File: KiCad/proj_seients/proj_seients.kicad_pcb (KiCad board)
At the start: 4 copper layers, 102 parts, among them J1 BATERIA 12V, J10 Screw_Terminal_01x05, J11 FCarrera, J12 FCarrera, J13 FCarrera, J14 FCarrera, J17 FCarrera, J19 J_SENSOR_TEMP, J2 5f0857756ylz, J3 DE9_Pins, J4 Motor, J5 Motor, J6 Motor, J7 Manta_Asiento, J8 DE9_Socket, J9 FCarrera, Q1 IRLZ44N, SW1 SW_Push, SW2 SW_Push, SW3 SW_Push, SW4 SW_Push, SW5 SW_Push, SW6 SW_Push, SW7 SW_Push, U1 PIC24HJ128GP502, U10 MAX3232, U11 PCF8574AP, U2 LM2596S-5, U3 LM1117DT-3.3, U4 MCP2562-E-SN, U5 PCA9685BS, U6 DRV8871DDA, U7 DRV8871DDA, U8 DRV8871DDA, U9 24LC256, Y1 8MHz

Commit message: Versió 1.0 Layout
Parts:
- moved C36 137.7 mm to (182.5, 144.9), turned to -90 degrees
- moved C17 131.7 mm to (137.1, 147.0)
- moved C18 124.4 mm to (135.1, 143.0)
- moved C28 120.3 mm to (152.9, 140.5), turned to 180 degrees
- moved C19 119.3 mm to (96.5, 144.0)
- moved C20 118.2 mm to (89.0, 145.0)
- moved C24 117.9 mm to (147.1, 128.0)
- moved C21 113.5 mm to (106.5, 144.5)
- moved C22 111.2 mm to (125.5, 143.5)
- moved C6 100.1 mm to (134.6, 113.5)
- moved R2 98.5 mm to (184.0, 91.9), turned to 90 degrees
- moved C11 98.4 mm to (182.1, 81.5)
- moved R4 98.2 mm to (175.5, 145.1), turned to -90 degrees
- moved C7 97.7 mm to (158.9, 101.0), turned to 180 degrees
- moved R7 96.9 mm to (182.0, 140.0)
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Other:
- copper layers 4 -> 2

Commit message: Versió 1.1 Layout
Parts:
- moved C9 80.2 mm to (101.0, 122.5), turned to -90 degrees
- moved C10 72.0 mm to (110.0, 123.5), turned to -90 degrees
- moved C8 64.0 mm to (119.0, 123.5), turned to -90 degrees
- moved J7 49.1 mm to (82.3, 94.5), turned to -90 degrees
- moved C36 38.9 mm to (145.0, 134.6), turned to 90 degrees
- moved R6 32.3 mm to (148.5, 134.4), turned to 90 degrees
- moved R4 25.8 mm to (152.0, 134.4), turned to 90 degrees
- moved R25 19.7 mm to (155.5, 134.4), turned to 90 degrees
- moved U5 12.7 mm to (162.7, 130.5)
- moved SW5 10.0 mm to (123.5, 139.0)
- moved C1 9.73 mm to (126.5, 119.5)
- moved C22 9.00 mm to (116.5, 143.5)
- moved SW6 9.00 mm to (114.5, 139.3)
- moved Q1 2.77 mm to (125.5, 80.0)
- moved J1 1.00 mm to (81.0, 110.4)
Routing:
- net 5V: track 0.00 -> 142.6 mm, vias 0 -> 3
- net Net-(U11-P2): track 0.00 -> 87.9 mm, vias 0 -> 2
- net 12V: track 0.00 -> 85.6 mm
- net Net-(U11-P4): track 0.00 -> 78.0 mm
- net Net-(U11-P3): track 0.00 -> 71.2 mm, vias 0 -> 2
- net I2C_SDA: track 0.00 -> 70.1 mm, vias 0 -> 2
- net Net-(U11-P5): track 0.00 -> 63.9 mm
- net LIM_REC_MIN: track 0.00 -> 59.5 mm, vias 0 -> 2
- net I2C_SCL: track 0.00 -> 57.9 mm, vias 0 -> 2
- net LIM_REC_MAX: track 0.00 -> 53.0 mm
- net Net-(J7-Pin_1): track 0.00 -> 48.2 mm
- net LIM_POS_MAX: track 0.00 -> 43.3 mm, vias 0 -> 2
- net Net-(U1-AVSS): track 0.00 -> 38.2 mm
- net Net-(U11-P0): track 0.00 -> 32.5 mm
- net Net-(J10-Pin_1): track 0.00 -> 32.2 mm
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
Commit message: Versió 2.0 Layout
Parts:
- moved J6 113.7 mm to (81.6, 133.0), turned to -90 degrees
- moved SW1 111.4 mm to (188.2, 127.5), turned to 0 degrees
- moved R5 103.5 mm to (188.5, 140.1), turned to -90 degrees
- moved SW3 85.9 mm to (173.0, 104.5), turned to 0 degrees
- moved J5 85.3 mm to (111.7, 142.9), turned to 0 degrees
- moved U6 83.9 mm to (100.1, 134.0), turned to 180 degrees
- moved R7 76.5 mm to (106.0, 131.1), turned to 90 degrees
- moved J4 74.8 mm to (126.2, 142.9), turned to 0 degrees
- moved SW2 73.1 mm to (158.8, 132.2), turned to 180 degrees
- moved C21 71.6 mm to (175.7, 126.1), turned to 90 degrees
- moved C19 69.3 mm to (158.5, 113.0), turned to -90 degrees
- moved SW4 67.2 mm to (170.5, 128.5), turned to 180 degrees
- moved C22 66.8 mm to (177.7, 116.7), turned to 90 degrees
- moved C20 62.7 mm to (149.5, 128.3), turned to -90 degrees
- moved SW6 62.5 mm to (173.5, 118.8), turned to 180 degrees
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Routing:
- net 5V: track 142.6 -> 0.00 mm, vias 3 -> 0
- net Net-(U11-P2): track 87.9 -> 0.00 mm, vias 2 -> 0
- net 12V: track 85.6 -> 0.00 mm
- net Net-(U11-P4): track 78.0 -> 0.00 mm
- net Net-(U11-P3): track 71.2 -> 0.00 mm, vias 2 -> 0
- net I2C_SDA: track 70.1 -> 0.00 mm, vias 2 -> 0
- net Net-(U11-P5): track 63.9 -> 0.00 mm
- net LIM_REC_MIN: track 59.5 -> 0.00 mm, vias 2 -> 0
- net I2C_SCL: track 57.9 -> 0.00 mm, vias 2 -> 0
- net LIM_REC_MAX: track 53.0 -> 0.00 mm
- net Net-(J7-Pin_1): track 48.2 -> 0.00 mm
- net LIM_POS_MAX: track 43.3 -> 0.00 mm, vias 2 -> 0
- net Net-(U1-AVSS): track 38.2 -> 0.00 mm
- net Net-(U11-P0): track 32.5 -> 0.00 mm
- net Net-(J10-Pin_1): track 32.2 -> 0.00 mm
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- added copper zone on B.Cu, net GND
- added copper zone on F.Cu, net GND

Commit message: Versió 2.1 Layout
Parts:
- moved C22 11.0 mm to (188.8, 117.0)
- moved SW3 10.6 mm to (183.2, 107.2)
- moved SW6 9.17 mm to (182.5, 120.5)
- moved C6 5.78 mm to (131.4, 108.7), turned to 90 degrees
- moved U9 4.27 mm to (169.0, 108.0)
- moved C17 3.45 mm to (168.3, 139.2), turned to 0 degrees
- moved C5 1.50 mm to (131.5, 102.0)
- moved R1 1.22 mm to (142.8, 112.9), turned to 90 degrees
- moved C24 1.00 mm to (143.8, 127.0)
- moved C19 0.70 mm to (159.2, 113.0)
- moved R23 0.67 mm to (152.0, 112.7), turned to -90 degrees
- moved R16 0.52 mm to (147.4, 112.9), turned to 90 degrees
- moved D1 0.51 mm to (93.0, 123.5)
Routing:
- net 3.3V: track 0.00 -> 416.8 mm, vias 0 -> 2
- net 5V: track 0.00 -> 177.9 mm
- net 12V: track 0.00 -> 136.5 mm
- net Net-(J10-Pin_1): track 0.00 -> 109.0 mm, vias 0 -> 4
- net I2C_SDA: track 0.00 -> 94.7 mm, vias 0 -> 5
- net I2C_SCL: track 0.00 -> 86.4 mm, vias 0 -> 2
- net CALEFACCIÓ: track 0.00 -> 78.7 mm, vias 0 -> 3
- net LIM_POS_MIN: track 0.00 -> 73.5 mm, vias 0 -> 2
- net LIM_AL_MIN: track 0.00 -> 70.1 mm, vias 0 -> 1
- net Net-(U11-P1): track 0.00 -> 52.7 mm, vias 0 -> 1
- net LIM_REC_MAX: track 0.00 -> 52.4 mm, vias 0 -> 1
- net LIM_REC_MIN: track 0.00 -> 51.8 mm, vias 0 -> 2
- net Net-(J7-Pin_1): track 0.00 -> 48.2 mm
- net CINT: track 0.00 -> 47.6 mm, vias 0 -> 2
- net Net-(U1-AVSS): track 0.00 -> 46.5 mm
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
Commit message: Versió 2.2 Layout
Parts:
- J3: footprint Connector_Dsub:DSUB-9_Pins_Vertical_P2.77x2.84mm -> Connector_Dsub:DSUB-9_Pins_Horizontal_P2.77x2.84mm_EdgePinOffset9.40mm
- J8: footprint Connector_Dsub:DSUB-9_Socket_Vertical_P2.77x2.84mm -> Connector_Dsub:DSUB-9_Socket_Horizontal_P2.77x2.84mm_EdgePinOffset9.40mm
- moved J8 12.9 mm to (151.9, 78.3), turned to 180 degrees
- moved J3 5.01 mm to (187.0, 94.8)
- moved REF** 3.10 mm to (197.1, 149.1)
- moved REF** 3.01 mm to (78.8, 149.0)
- moved REF** 0.80 mm to (79.0, 67.7)
- moved REF** 0.30 mm to (197.0, 68.2)
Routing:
- net RX: track 45.2 -> 40.0 mm
- net CAN_H: track 30.0 -> 24.8 mm
- net CAN_L: track 27.1 -> 22.0 mm
- net TX: track 37.3 -> 39.3 mm
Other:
- board text added: "23/3/2026"
- board text added: "Autors: Miguel Tovar i Pol Salas PCB del circuit"
- board text added: "Placa de Control - Seients Elèctrics"
- board text added: "V2.2"

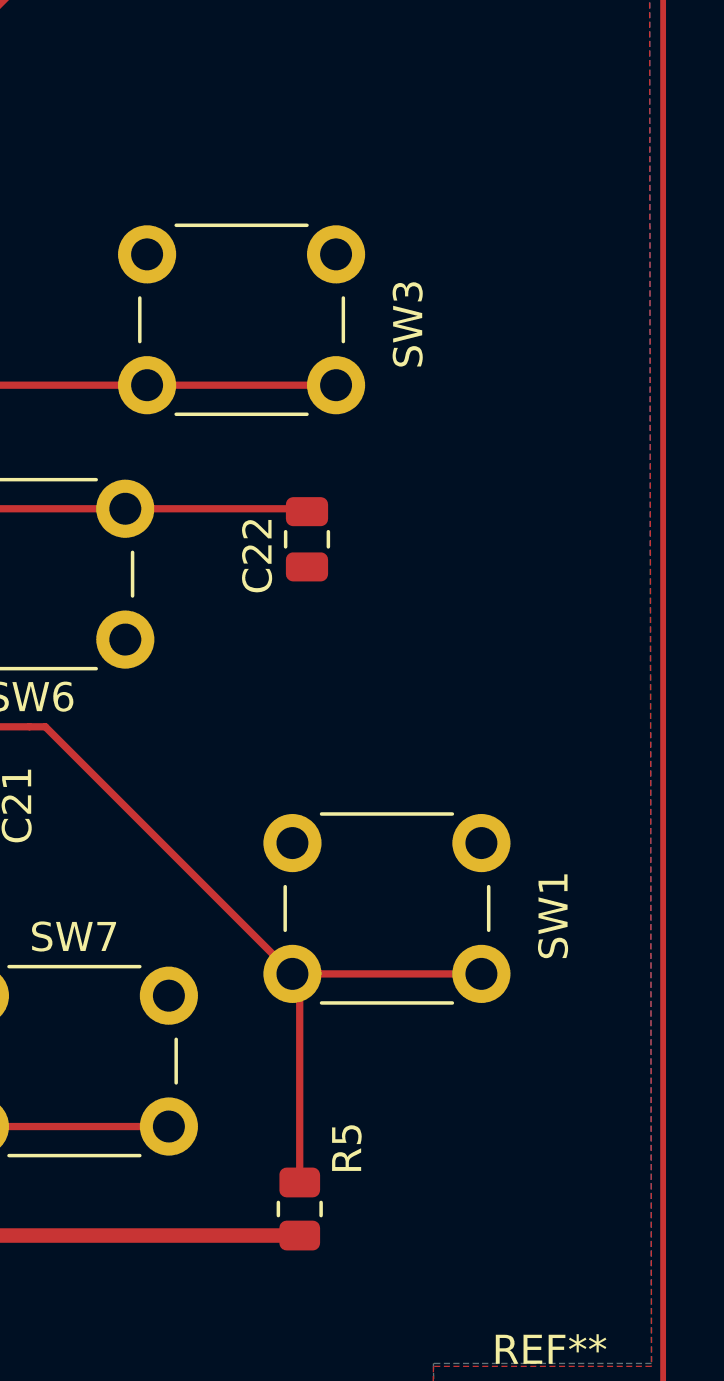
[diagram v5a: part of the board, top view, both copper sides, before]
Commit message: Afegit títol i autors a la placa
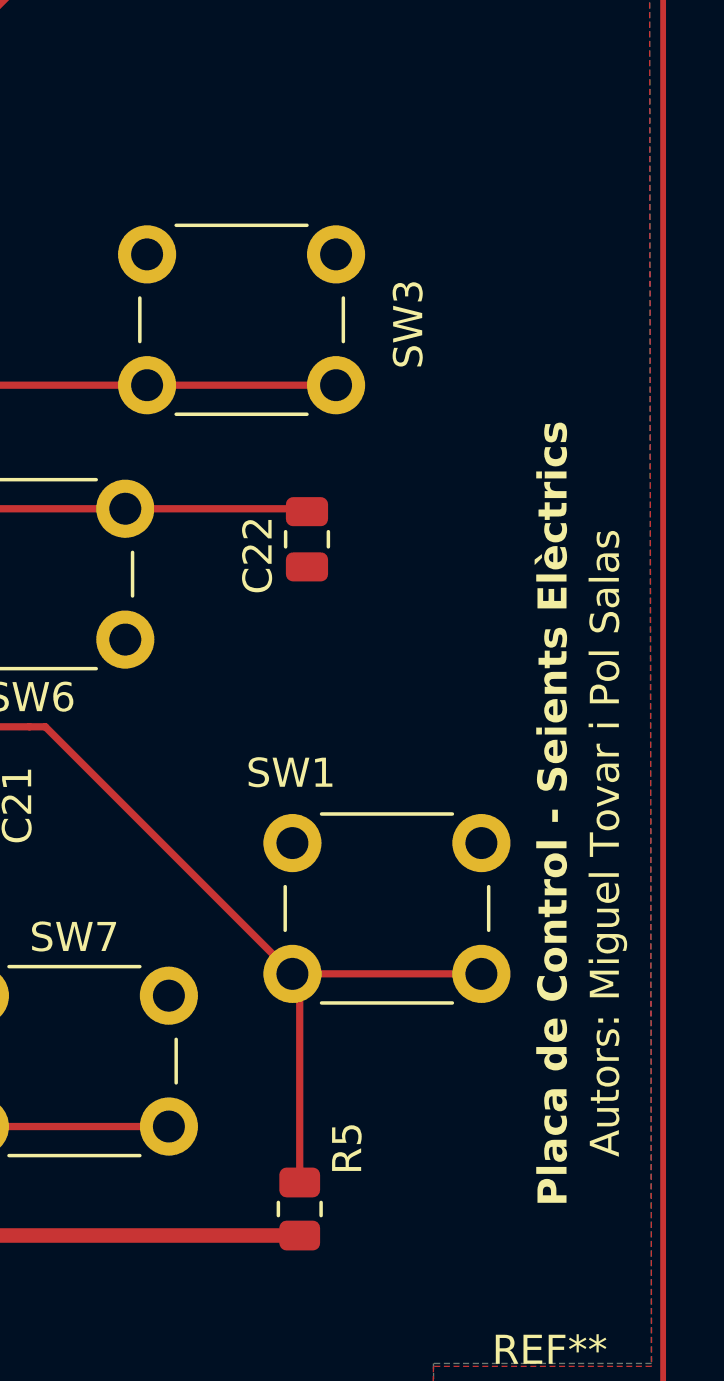
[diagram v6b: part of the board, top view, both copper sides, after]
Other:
- board text added: "Autors: Miguel Tovar i Pol Salas"
- board text removed: "23/3/2026"
- board text removed: "Autors: Miguel Tovar i Pol Salas PCB del circuit"
- board text removed: "V2.2"
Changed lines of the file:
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@@
 		(tags "tact sw push 6mm")
 		(property "Reference" "SW1"
-			(at 9 2.5 90)
+			(at -0.05 -2.4 180)
 			(layer "F.SilkS")
 			(effects
@@
 		(layer "F.Cu")
 	)
-	(gr_text "V2.2"
-		(at 268.5 194.2 0)
-		(layer "Cmts.User")
+	(gr_text "Placa de Control - Seients Elèctrics"
+		(at 197.8 140 90)
+		(layer "F.SilkS")
 		(effects
 			(font
-				(size 1.5 1.5)
-				(thickness 0.3)
+				(size 1 1)
+				(thickness 0.25)
 				(bold yes)
 			)
@@
 		)
 	)
-	(gr_text "23/3/2026\n"
-		(at 206.8 194.1 0)
-		(layer "Cmts.User")
+	(gr_text "Autors: Miguel Tovar i Pol Salas\n"
+		(at 199.6 138.3 90)
+		(layer "F.SilkS")
 		(effects
 			(font
-				(size 1.5 1.5)
-				(thickness 0.3)
-				(bold yes)
+				(size 1 1)
+				(thickness 0.25)
 			)
 			(justify left bottom)
-		)
-	)
-	(gr_text "Autors: Miguel Tovar i Pol Salas\nPCB del circuit"
-		(at 177.9 178.3 0)
-		(layer "Cmts.User")
-		(effects
-			(font
-				(size 3 3)
-				(thickness 0.75)
-			)
-			(justify left bottom)
-		)
-	)
-	(gr_text "Placa de Control - Seients Elèctrics"
-		(at 186.5 190.4 0)
-		(layer "Cmts.User")
-		(effects
-			(font
-				(size 1.5 1.5)
-				(thickness 0.3)
-				(bold yes)
-			)
-			(justify left bottom)

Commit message: Version V2.4
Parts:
- moved U10 1.17 mm to (164.0, 88.5)
- moved C7 1.05 mm to (160.0, 101.0)
- moved U4 1.00 mm to (166.5, 98.5)
- turned C20 to 90 degrees
- turned R9 to 90 degrees
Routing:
- net I2C_SCL: track 86.4 -> 101.0 mm, vias 2 -> 3
- net I2C_SDA: track 94.7 -> 104.0 mm, vias 5 -> 6
- net 5V: track 177.9 -> 170.0 mm
- net Net-(J7-Pin_1): track 48.2 -> 55.2 mm
- net Net-(U6-ILIM): track 0.00 -> 3.06 mm
- net 3.3V: track 416.8 -> 414.3 mm
- net Net-(D3-A): track 0.00 -> 2.50 mm
- net UART_RX: track 25.7 -> 27.0 mm
- net UART_TX: track 23.9 -> 25.2 mm
- net Net-(U10-VS+): track 4.41 -> 3.16 mm
- net Net-(U10-C2-): track 4.38 -> 3.12 mm
- net Net-(U10-C2+): track 4.64 -> 3.38 mm
- net Net-(U1-VCAP): track 3.88 -> 4.93 mm
- net CAN_H: track 24.8 -> 23.8 mm
- net CAN_L: track 22.0 -> 21.0 mm
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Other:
- board outline added: 126 x 89.4 mm

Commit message: V2.5
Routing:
- net 5V: track 170.0 -> 177.1 mm
- net Net-(J7-Pin_1): track 55.2 -> 50.6 mm
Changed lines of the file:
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@@
 	)
 	(gr_line
+		(start 89.8 98.6)
+		(end 89.7 85.1)
+		(stroke
+			(width 0.6)
+			(type solid)
+		)
+		(layer "F.Cu")
+	)
+	(gr_line
 		(start 120 115)
 		(end 120 116.5)
@@
 	)
 	(gr_line
+		(start 119.9 100)
+		(end 119.9 90.8)
+		(stroke
+			(width 0.6)
+			(type solid)
+		)
+		(layer "F.Cu")
+	)
+	(gr_line
+		(start 119.9 90.8)
+		(end 119.9 85.1)
+		(stroke
+			(width 0.6)
+			(type solid)
+		)
+		(layer "F.Cu")
+	)
+	(gr_line
 		(start 120 110.9)
 		(end 120 115)
@@
 		(layer "F.Cu")
 	)
+	(gr_line
+		(start 119.9 105.06)
+		(end 119.9 100)
+		(stroke
+			(width 0.6)
+			(type solid)
+		)
+		(layer "F.Cu")
+	)
+	(gr_line
+		(start 119.9 85.1)
+		(end 99.2 85.1)
+		(stroke
+			(width 0.6)
+			(type solid)
+		)
+		(layer "F.Cu")
+	)
+	(gr_line
+		(start 89.7 85.1)
+		(end 99.2 85.1)
+		(stroke
+			(width 0.6)
+			(type solid)
+		)
+		(layer "F.Cu")
+	)
 	(gr_rect
 		(start 75 63.6)
@@
 	)
 	(via
-		(at 122.5 97.5)
+		(at 93.5 80.9)
 		(size 0.6)
 		(drill 0.3)
@@
 	)
 	(segment
-		(start 93.625 72.295)
+		(start 93.2 70.3)
 		(end 93.625 70.725)
 		(width 0.5)
@@
 	)
 	(segment
-		(start 80.2 92.1)
+		(start 81 96.7)
 		(end 80.2 95.9)
 		(width 0.5)
@@
 	)
 	(segment
-		(start 93.625 70.725)
-		(end 93.2 70.3)
+		(start 103.991215 94.525)
+		(end 102.971349 93.505134)
 		(width 0.5)
 		(layer "F.Cu")
@@
 	)
 	(segment
+		(start 89.5 100)
+		(end 86.9 100)
+		(width 0.5)
+		(layer "F.Cu")
+		(net 3)
+	)
+	(segment
 		(start 96.905 72.295)
 		(end 97.5 71.7)
@@
 	)
 	(segment
+		(start 86.9 100)
+		(end 83.6 96.7)
+		(width 0.5)
+		(layer "F.Cu")
+		(net 3)
+	)
+	(segment
 		(start 156.026 108.774)
 		(end 154.8 110)
@@
 	)
 	(segment
+		(start 102.971349 91.103134)
+		(end 101.468215 89.6)
+		(width 0.5)
+		(layer "F.Cu")
+		(net 3)
+	)
+	(segment
 		(start 117.8 98.2)
 		(end 114.125 94.525)
@@
 	)
 	(segment
-		(start 93.2 70.3)
-		(end 83.7 70.3)
+		(start 105.922349 94.525)
+		(end 103.991215 94.525)
 		(width 0.5)
 		(layer "F.Cu")
@@
 	)
 	(segment
-		(start 91.9 89.6)
-		(end 101.468215 89.6)
+		(start 114.125 94.525)
+		(end 105.922349 94.525)
 		(width 0.5)
 		(layer "F.Cu")
@@
 	)
 	(segment
-		(start 102.971349 93.505134)
-		(end 103.991215 94.525)
+		(start 93.625 72.295)
+		(end 96.905 72.295)
 		(width 0.5)
 		(layer "F.Cu")
@@
 	)
 	(segment
-		(start 114.125 94.525)
-		(end 105.922349 94.525)
+		(start 83.3 70.7)
+		(end 83.7 70.3)
 		(width 0.5)
 		(layer "F.Cu")
@@
 	)
 	(segment
-		(start 93.625 72.295)
-		(end 96.905 72.295)
+		(start 131.4 114.2)
+		(end 127.2 110)
 		(width 0.5)
 		(layer "F.Cu")
@@
 	)
 	(segment
-		(start 131.4 114.2)
-		(end 127.2 110)
+		(start 93.625 70.725)
+		(end 93.625 72.295)
 		(width 0.5)
 		(layer "F.Cu")
@@
 	)
 	(segment
-		(start 156.026 103.867498)
-		(end 156.026 108.774)
+		(start 101.468215 89.6)
+		(end 91.9 89.6)
 		(width 0.5)
 		(layer "F.Cu")
@@
 	)
 	(segment
-		(start 101.468215 89.6)
-		(end 102.971349 91.103134)
+		(start 90.6 98.9)
+		(end 89.5 100)
 		(width 0.5)
 		(layer "F.Cu")
@@
 	)
 	(segment
-		(start 162.5 102.5)
-		(end 161.701 103.299)
+		(start 156.026 103.867498)
+		(end 156.026 108.774)
 		(width 0.5)
 		(layer "F.Cu")
@@
 	)
 	(segment
-		(start 84.4 97.1)
-		(end 91.9 89.6)
+		(start 83.7 70.3)
+		(end 93.2 70.3)
 		(width 0.5)
 		(layer "F.Cu")
@@
 	)
 	(segment
-		(start 83.7 70.3)
-		(end 83.3 70.7)
+		(start 102.971349 93.505134)
+		(end 102.971349 91.103134)
 		(width 0.5)
 		(layer "F.Cu")
@@
 	)
 	(segment
-		(start 81.4 97.1)
-		(end 84.4 97.1)
+		(start 90.6 90.9)
+		(end 90.6 98.9)
 		(width 0.5)
 		(layer "F.Cu")
@@
 	)
 	(segment
-		(start 102.971349 91.103134)
-		(end 102.971349 93.505134)
+		(start 80.2 95.9)
+		(end 80.2 92.1)
 		(width 0.5)
 		(layer "F.Cu")
@@
 	)
 	(segment
-		(start 109.5 109)
-		(end 110.75 109)
+		(start 80.2 92.1)
+		(end 83.3 89)
 		(width 0.5)
 		(layer "F.Cu")
@@
 	)
 	(segment
-		(start 83.3 70.7)
-		(end 83.3 89)
+		(start 91.9 89.6)
+		(end 90.6 90.9)
 		(width 0.5)
 		(layer "F.Cu")
@@
 	)
 	(segment
-		(start 117.8 105.3)
-		(end 117.8 98.2)
+		(start 162.5 102.5)
+		(end 161.701 103.299)
 		(width 0.5)
 		(layer "F.Cu")
@@
 	)
 	(segment
-		(start 80.2 95.9)
-		(end 81.4 97.1)
+		(start 83.6 96.7)
+		(end 81 96.7)
 		(width 0.5)
 		(layer "F.Cu")
@@
 	)
 	(segment
-		(start 103.991215 94.525)
-		(end 105.922349 94.525)
+		(start 109.5 109)
+		(end 110.75 109)
 		(width 0.5)
 		(layer "F.Cu")
@@
 	)
 	(segment
-		(start 121.5 109)
-		(end 117.8 105.3)
+		(start 117.8 105.3)
+		(end 117.8 98.2)
 		(width 0.5)
 		(layer "F.Cu")
@@
 	(segment
 		(start 83.3 89)
-		(end 80.2 92.1)
+		(end 83.3 70.7)
+		(width 0.5)
+		(layer "F.Cu")
+		(net 3)
+	)
+	(segment
+		(start 121.5 109)
+		(end 117.8 105.3)
 		(width 0.5)
 		(layer "F.Cu")
@@
 	)
 	(segment
-		(start 87 88.5)
-		(end 106.5 88.5)
+		(start 82.3275 91.8725)
+		(end 88.5 85.7)
 		(width 0.25)
 		(layer "F.Cu")
@@
 	)
 	(segment
-		(start 122.96 89.04)
-		(end 122.96 80)
+		(start 88.5 85.7)
+		(end 88.5 84.8)
 		(width 0.25)
 		(layer "F.Cu")
@@
 	)
 	(segment
-		(start 106.5 88.5)
-		(end 109.5 91.5)
+		(start 122 84.2)
+		(end 122.96 83.24)
 		(width 0.25)
 		(layer "F.Cu")
@@
 	(segment
 		(start 82.3275 94.455)
-		(end 82.3275 93.1725)
+		(end 82.3275 91.8725)
 		(width 0.25)
 		(layer "F.Cu")
@@
 	)
 	(segment
-		(start 120.5 91.5)
-		(end 122.96 89.04)
+		(start 122.96 83.24)
+		(end 122.96 80)
 		(width 0.25)
 		(layer "F.Cu")
@@
 	)
 	(segment
-		(start 109.5 91.5)
-		(end 120.5 91.5)
+		(start 88.5 84.8)
+		(end 89.1 84.2)
 		(width 0.25)
 		(layer "F.Cu")
@@
 	)
 	(segment
-		(start 82.3275 93.1725)
-		(end 87 88.5)
+		(start 89.1 84.2)
+		(end 122 84.2)
 		(width 0.25)
 		(layer "F.Cu")
@@
 			)
 		)
+	)
+	(zone
+		(net 4)
+		(net_name "3.3V")
+		(layer "F.Cu")
+		(name "$teardrop_track$")
+		(hatch none 0.1)
+		(priority 30000)
+		(attr
+			(teardrop
+				(type track_end)
+			)
+		)
+		(connect_pads yes
+			(clearance 0)
+		)
+		(min_thickness 0.0254)
+		(filled_areas_thickness no)
+		(fill yes
+			(thermal_gap 0.5)
+			(thermal_bridge_width 0.5)
+			(island_removal_mode 1)
+			(island_area_min 10)
+		)
+		(polygon
+			(pts
+				(xy 103.679 146.104804) (xy 103.674346 146.191791) (xy 103.661765 146.256764) (xy 103.623162 146.352037)
+				(xy 103.587662 146.432723) (xy 103.554804 146.551227) (xy 103.8 146.601) (xy 104.045196 146.551227)
+				(xy 103.999541 146.396891) (xy 103.981198 146.354578) (xy 103.944372 146.255434) (xy 103.933133 146.190826)
+				(xy 103.929 146.104804)
+			)
+		)
